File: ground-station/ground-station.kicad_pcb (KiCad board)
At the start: 4 copper layers, 65.5 x 32 mm, 32 parts, among them J1 SMA_Coax, J2 USB_C_Receptacle_USB2.0_16P, J3 Conn_01x03, U1 FT230XS, U2 RN2903, U3 LM3671MF, U4 USBLC6-2SC6

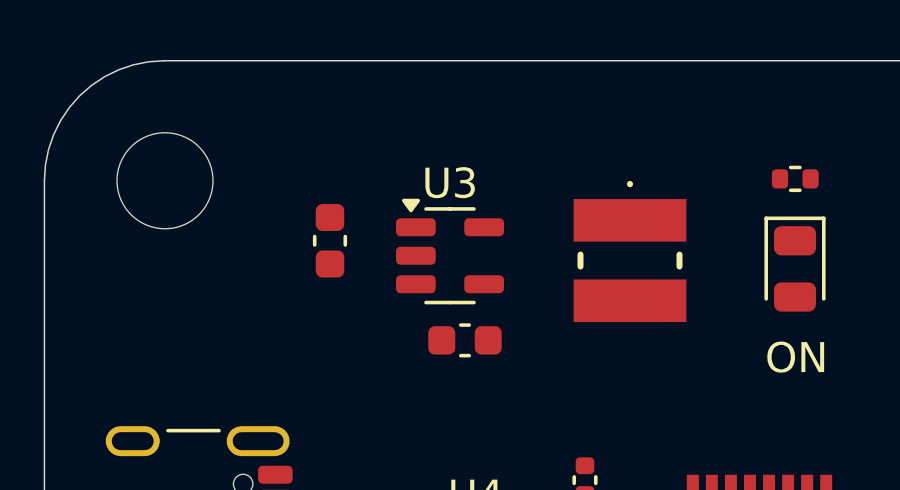
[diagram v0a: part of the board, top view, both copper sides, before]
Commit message: Modified paste layer
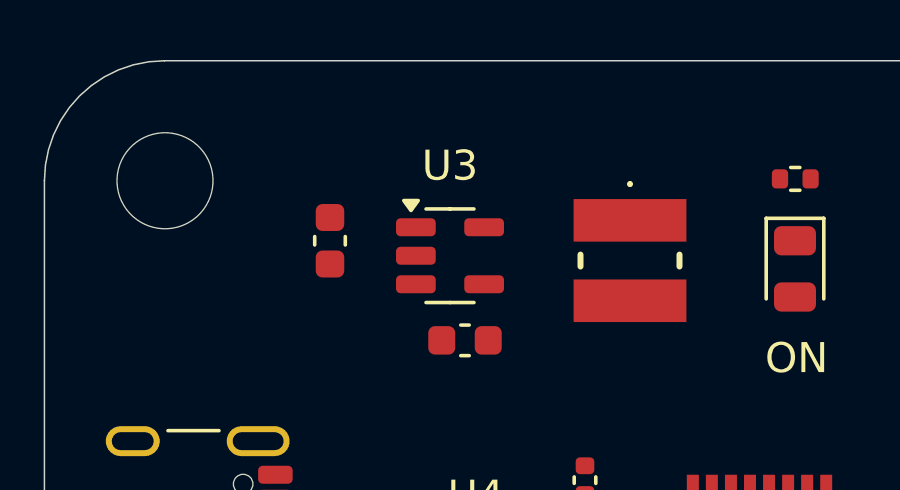
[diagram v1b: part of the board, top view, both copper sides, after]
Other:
- board text added: "Matteo Golin"

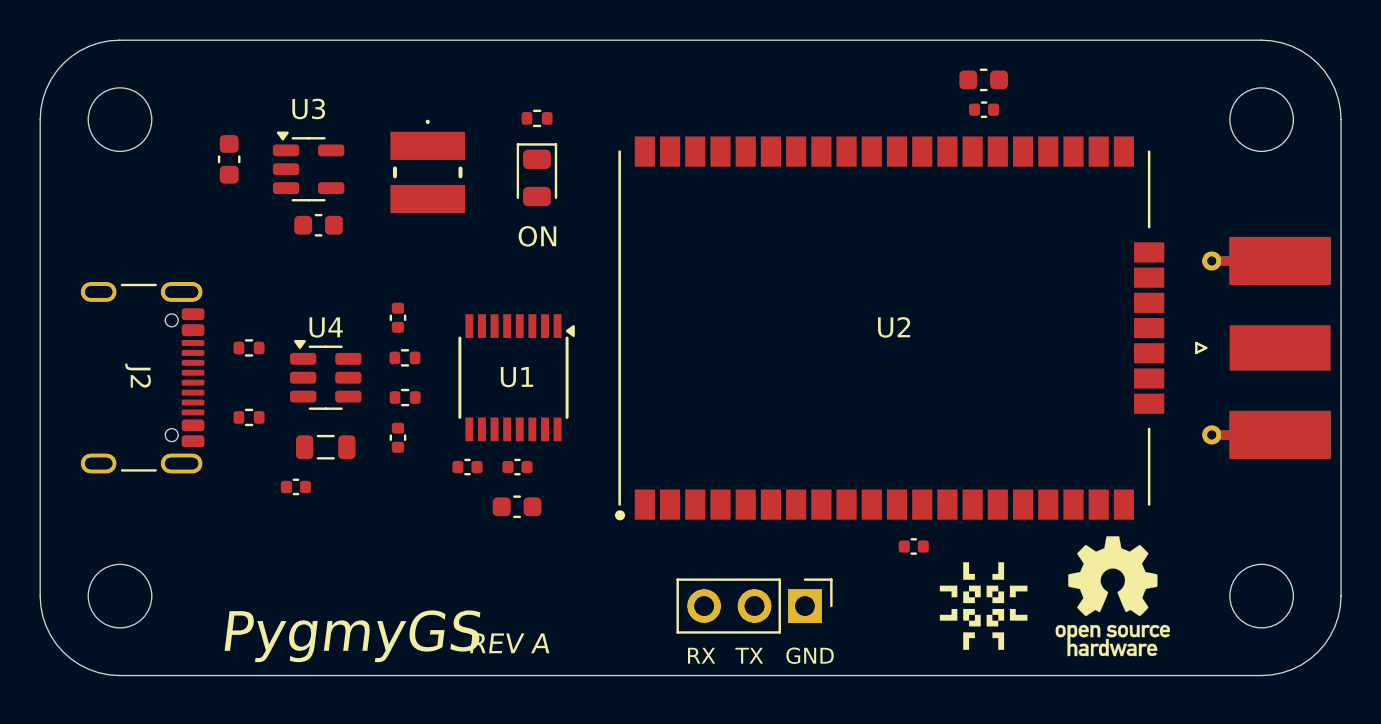
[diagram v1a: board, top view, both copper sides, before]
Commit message: Routing finished for ground station.
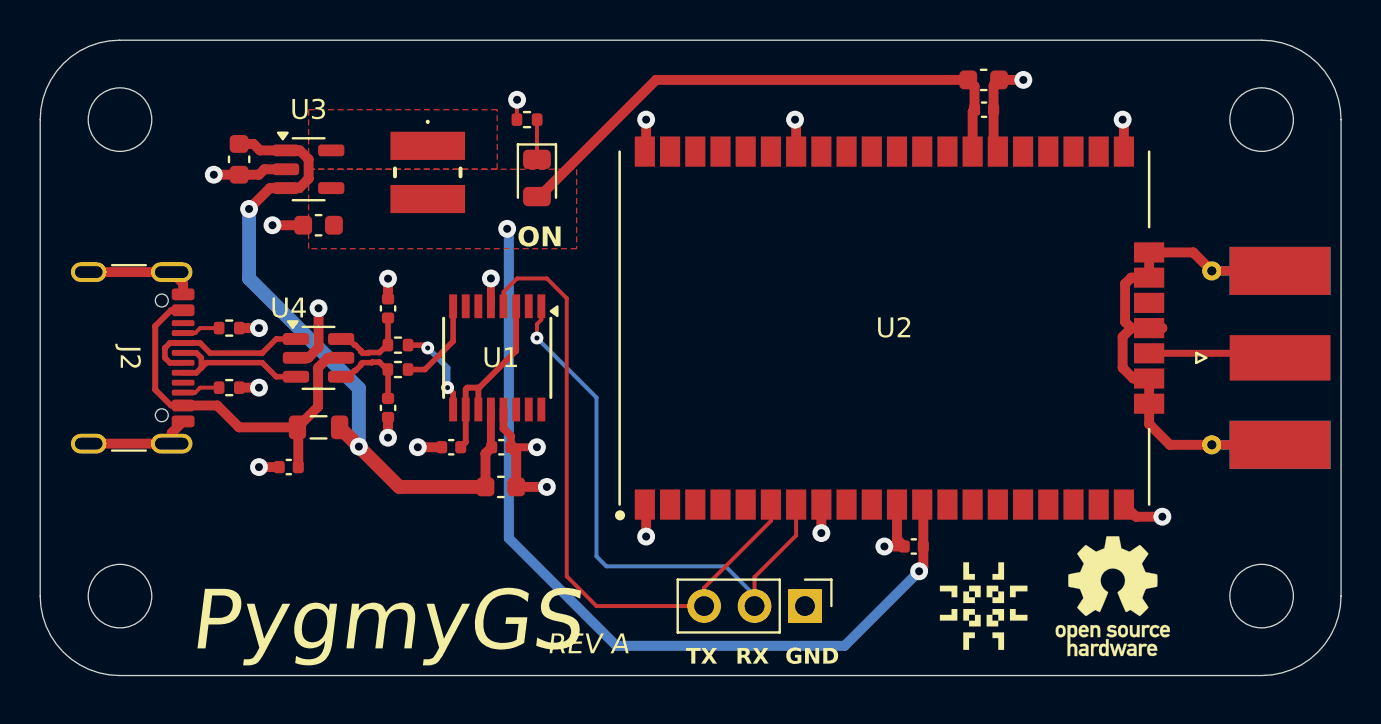
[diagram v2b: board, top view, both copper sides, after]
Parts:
- moved R4 1.80 mm to (112.0, 100.5)
- moved C7 1.58 mm to (120.0, 101.5)
- moved R2 1.46 mm to (120.5, 99.6)
- moved R3 1.41 mm to (112.0, 97.5)
- moved C1 1.29 mm to (125.7, 103.5)
- moved C2 1.29 mm to (125.7, 105.5)
- moved C8 1.29 mm to (123.2, 103.5)
- moved U1 1.29 mm to (125.5, 99.0)
- moved J2 1.12 mm to (106.0, 99.0)
- moved C11 1.06 mm to (115.0, 104.5)
- moved FB1 1.06 mm to (116.5, 102.5)
- moved U4 1.06 mm to (116.5, 99.0)
- moved R1 0.73 mm to (120.5, 98.4)
- moved C6 0.69 mm to (120.0, 96.5)
- moved R5 0.51 mm to (127.0, 87.0)
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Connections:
- net Net-(U3-SW) renamed /PWR_NSY
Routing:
- net GND: track 0.00 -> 75.1 mm, vias 0 -> 21
- net +3V3: track 0.00 -> 71.5 mm, vias 0 -> 2
- net +5V: track 0.00 -> 35.3 mm, vias 0 -> 2
- net MCU_RX: track 0.00 -> 32.6 mm
- net MCU_TX: track 0.00 -> 29.2 mm, vias 0 -> 1
- net VBUS: track 0.00 -> 19.7 mm
- net Net-(U1-3V3OUT): track 0.00 -> 9.70 mm
- net /D-: track 0.00 -> 8.73 mm
- net /D+: track 0.00 -> 7.71 mm
- net /RF_SIG: track 0.00 -> 6.69 mm
- net /RD-: track 0.00 -> 4.68 mm, vias 0 -> 2
- net /RD+: track 0.00 -> 4.62 mm
- net /MCU_D+: track 0.00 -> 4.31 mm
- net /MCU_D-: track 0.00 -> 4.24 mm
- net Net-(D1-K): track 0.00 -> 2.00 mm
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- added copper zone on F.Cu, net +3V3
- added copper zone on F.Cu, net /PWR_NSY
- added copper zone on In1.Cu, net GND
- added copper zone on In2.Cu, net GND
